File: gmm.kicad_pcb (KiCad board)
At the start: 6 copper layers, 55 x 50 mm, 212 parts, among them P1 10144518-061802LF, P2 10144518-061802LF, P3 10144518-061802LF, P4 10144518-101802LF, U1 CCGM1A1, U10 PCA9539AHF, U11 TPS3840DL28DBV, U2 5P49V6965, U3 LM26480SQ, U4 STG3692, U5 STG3692, U6 74LVC1G08, U7 74LVC1G07, U8 STG3692, U9 IS25LQ032B-JNLE, Y1 NX3225SA

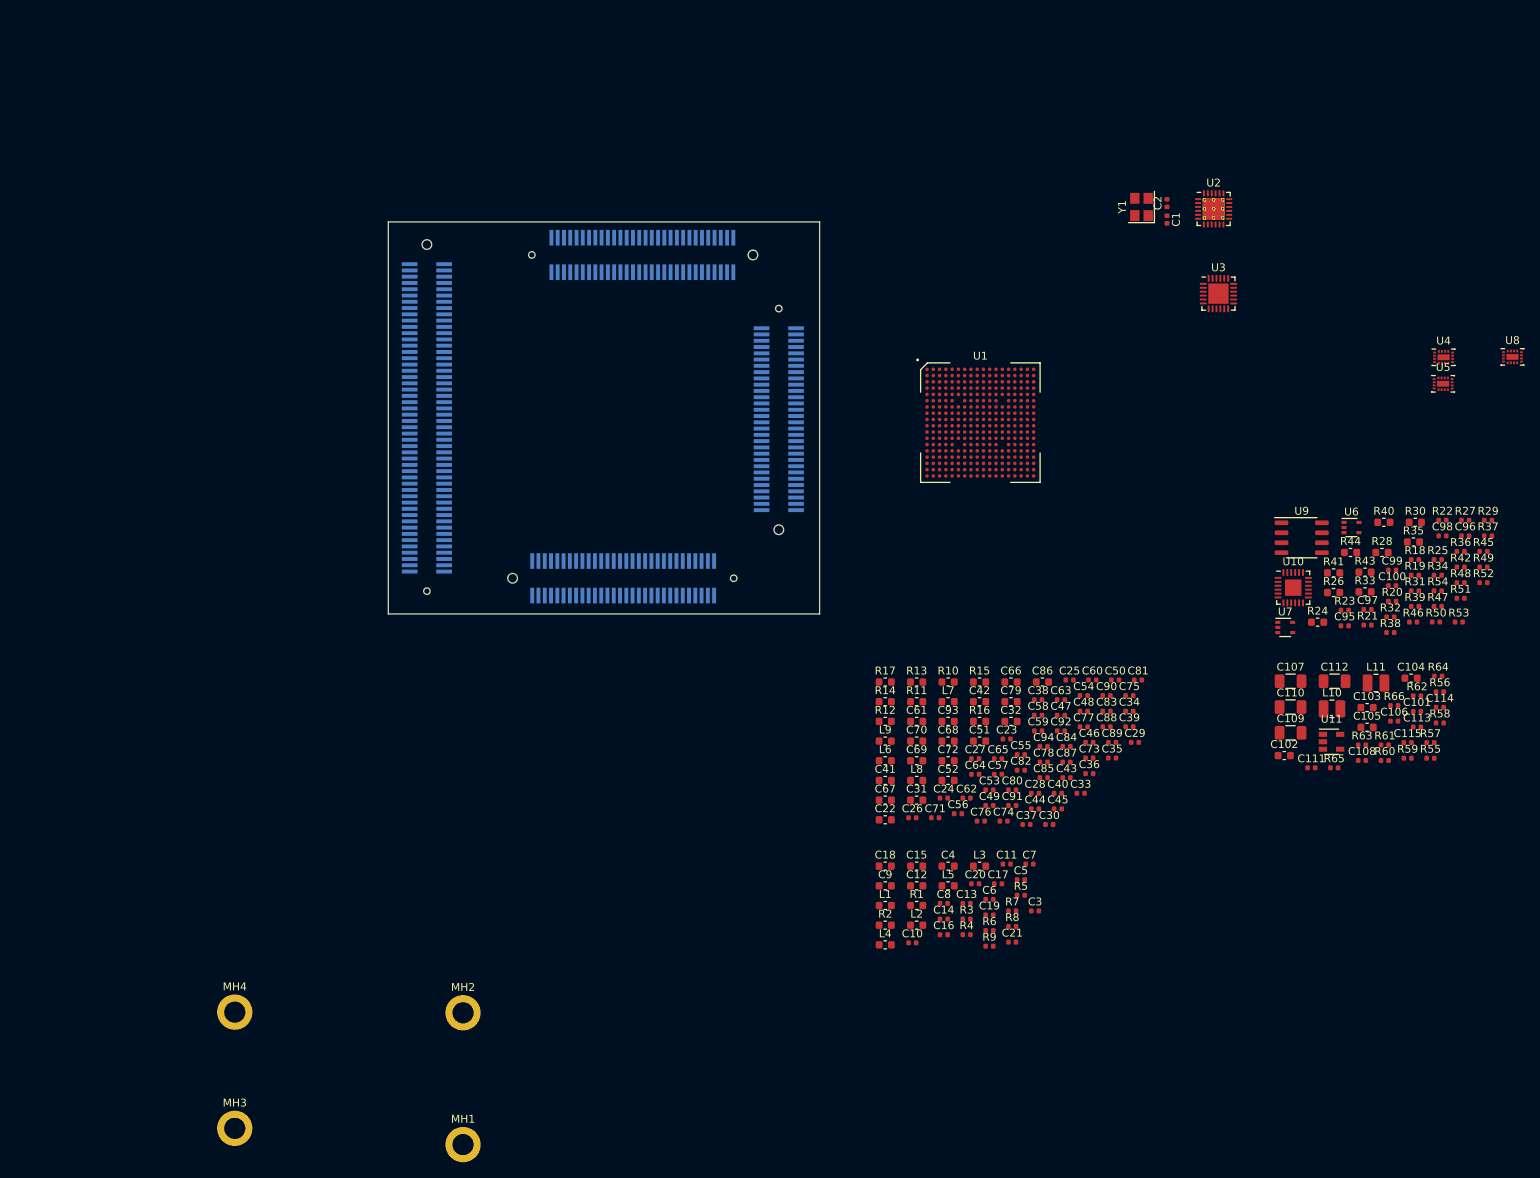
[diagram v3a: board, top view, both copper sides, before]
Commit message: Switch to five identical connectors, draft IO connection, current working PCB size is 50 x 75 mm
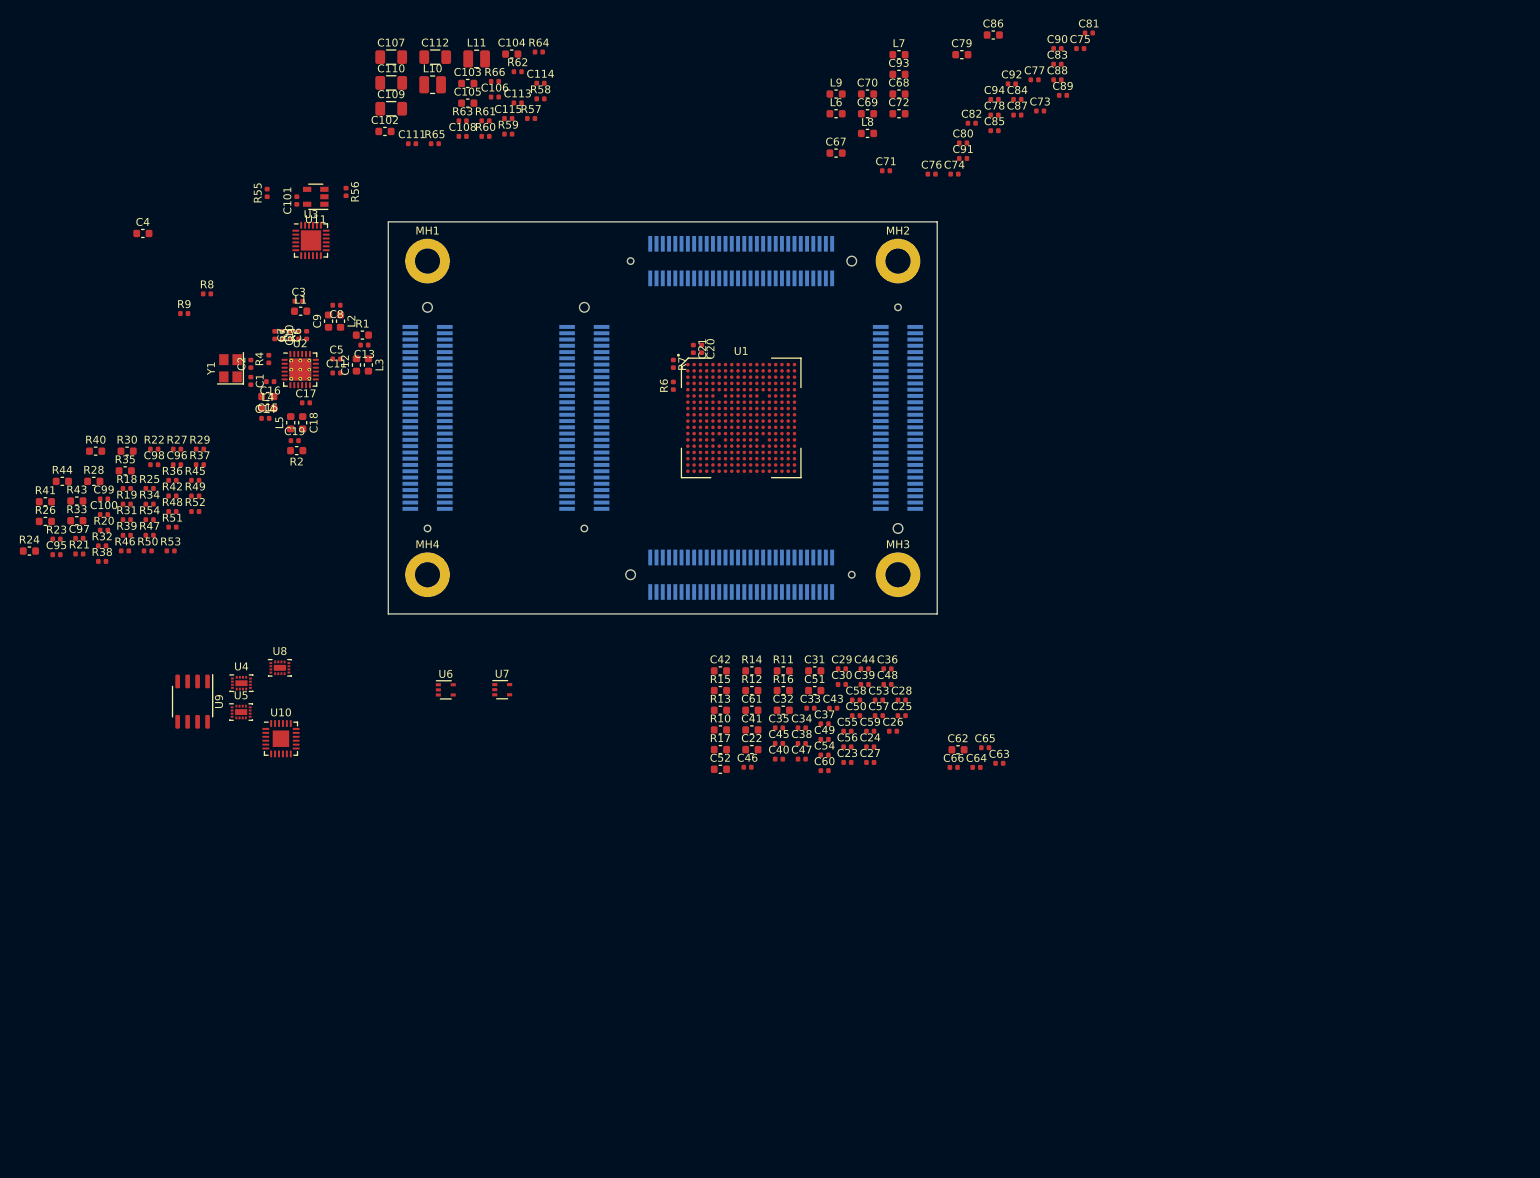
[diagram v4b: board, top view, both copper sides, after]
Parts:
- added P5: 10144518-061802LF, Amphenol:10144518-061802LF, B.Cu at (95.0, 105.0)
- C62: value 0.01uF -> 1.0uF; footprint Capacitor_SMD:C_0402_1005Metric -> Capacitor_SMD:C_0603_1608Metric
- C66: value 1.0uF -> 0.01uF; footprint Capacitor_SMD:C_0603_1608Metric -> Capacitor_SMD:C_0402_1005Metric
- MH1, MH2, MH3, MH4: footprint MountingHole:MountingHole_2.7mm_M2.5_ISO14580_Pad -> MountingHole:MountingHole_3.2mm_M3_ISO7380_Pad
- P4: value 10144518-101802LF -> 10144518-061802LF; footprint Amphenol:10144518-101802LF -> Amphenol:10144518-061802LF
- moved R55 164.9 mm to (74.5, 76.3), turned to 90 degrees
- moved R50 164.5 mm to (59.3, 122.0)
- moved C100 164.5 mm to (53.7, 117.3)
- moved C95 164.5 mm to (47.7, 122.4)
- moved C96 164.5 mm to (63.1, 111.0)
- moved C97 164.5 mm to (50.6, 120.4)
- moved C98 164.5 mm to (60.1, 111.0)
- moved C99 164.5 mm to (53.7, 115.3)
- moved R18 164.5 mm to (56.6, 114.0)
- moved R19 164.5 mm to (56.6, 116.0)
- moved R20 164.5 mm to (53.7, 119.3)
- moved R21 164.5 mm to (50.6, 122.3)
- moved R22 164.5 mm to (60.1, 109.0)
- moved R23 164.5 mm to (47.7, 120.5)
- moved R24 164.5 mm to (44.2, 122.0)
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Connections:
- C22 pad 1: VIO_N1 -> VIO_W1
- C23 pad 1: VIO_N1 -> VIO_W1
- C24 pad 1: VIO_N1 -> VIO_W1
- C25 pad 1: VIO_N1 -> VIO_W1
- C26 pad 1: VIO_N1 -> VIO_W1
- C27 pad 1: VIO_E1 -> VIO_W2
- C28 pad 1: VIO_E1 -> VIO_W2
- C29 pad 1: VIO_E1 -> VIO_W2
- C30 pad 1: VIO_E1 -> VIO_W2
- C31 pad 1: VIO_E1 -> VIO_W2
- C32 pad 1: VIO_N2 -> VIO_N1
- C33 pad 1: VIO_N2 -> VIO_N1
- C34 pad 1: VIO_N2 -> VIO_N1
- C35 pad 1: VIO_N2 -> VIO_N1
- C36 pad 1: VIO_N2 -> VIO_N1
- C37 pad 1: VIO_E2 -> VIO_N2
- C38 pad 1: VIO_E2 -> VIO_N2
- C39 pad 1: VIO_E2 -> VIO_N2
- C40 pad 1: VIO_E2 -> VIO_N2
- C41 pad 1: VIO_E2 -> VIO_N2
- C42 pad 1: VIO_W1 -> VIO_E1
- C43 pad 1: VIO_W1 -> VIO_E1
- C44 pad 1: VIO_W1 -> VIO_E1
- C45 pad 1: VIO_W1 -> VIO_E1
- C46 pad 1: VIO_W1 -> VIO_E1
- C47 pad 1: VIO_S1 -> VIO_E2
- C48 pad 1: VIO_S1 -> VIO_E2
- C49 pad 1: VIO_S1 -> VIO_E2
- C50 pad 1: VIO_S1 -> VIO_E2
- C51 pad 1: VIO_S1 -> VIO_E2
- C52 pad 1: VIO_W2 -> VIO_S1
- C53 pad 1: VIO_W2 -> VIO_S1
- C54 pad 1: VIO_W2 -> VIO_S1
- C55 pad 1: VIO_W2 -> VIO_S1
- C56 pad 1: VIO_W2 -> VIO_S1
- P1 pad 1: (no net) -> GND
- P1 pad 10: (no net) -> IO_N1_A2
- P1 pad 11: (no net) -> IO_N1_B3
- P1 pad 12: (no net) -> IO_N1_B2
- P1 pad 13: (no net) -> GND
- P1 pad 14: (no net) -> GND
- P1 pad 15: (no net) -> IO_N1_A5
- P1 pad 16: (no net) -> IO_N1_A4
- P1 pad 17: (no net) -> IO_N1_B5
- P1 pad 18: (no net) -> IO_N1_B4
- P1 pad 19: (no net) -> GND
- P1 pad 2: (no net) -> GND
- P1 pad 20: (no net) -> GND
- P1 pad 21: (no net) -> IO_N1_A7
- P1 pad 22: (no net) -> IO_N1_A6
- P1 pad 23: (no net) -> IO_N1_B7
- P1 pad 24: (no net) -> IO_N1_B6
- P1 pad 25: (no net) -> GND
- P1 pad 26: (no net) -> GND
- P1 pad 27: (no net) -> IO_N2_B0
- P1 pad 28: (no net) -> IO_N1_A8
- P1 pad 29: (no net) -> IO_N2_A0
- P1 pad 3: (no net) -> IO_N1_A1
- P1 pad 30: (no net) -> IO_N1_B8
- P1 pad 31: (no net) -> VIO_N1
- P1 pad 32: (no net) -> VIO_N1
- P1 pad 33: (no net) -> +2V5
- P1 pad 34: (no net) -> +2V5
- P1 pad 35: (no net) -> VIO_N2
- P1 pad 36: (no net) -> VIO_N2
- P1 pad 37: (no net) -> IO_N2_B2
- P1 pad 38: (no net) -> IO_N2_B1
- P1 pad 39: (no net) -> IO_N2_A2
- P1 pad 4: (no net) -> IO_N1_A0
- P1 pad 40: (no net) -> IO_N2_A1
- P1 pad 41: (no net) -> GND
- P1 pad 42: (no net) -> GND
- P1 pad 43: (no net) -> IO_N2_B4
- P1 pad 44: (no net) -> IO_N2_B3
- P1 pad 45: (no net) -> IO_N2_A4
- P1 pad 46: (no net) -> IO_N2_A3
- P1 pad 47: (no net) -> GND
- P1 pad 48: (no net) -> GND
- P1 pad 49: (no net) -> IO_N2_B6
- P1 pad 5: (no net) -> IO_N1_B1
- P1 pad 50: (no net) -> IO_N2_B5
- P1 pad 51: (no net) -> IO_N2_A6
- P1 pad 52: (no net) -> IO_N2_A5
- P1 pad 53: (no net) -> GND
- P1 pad 54: (no net) -> GND
- P1 pad 55: (no net) -> IO_N2_B8
- P1 pad 56: (no net) -> IO_N2_B7
- P1 pad 57: (no net) -> IO_N2_A8
- P1 pad 58: (no net) -> IO_N2_A7
- P1 pad 59: (no net) -> GND
- P1 pad 6: (no net) -> IO_N1_B0
- P1 pad 60: (no net) -> GND
- P1 pad 7: (no net) -> GND
- P1 pad 8: (no net) -> GND
- P1 pad 9: (no net) -> IO_N1_A3
- P2 pad 1: (no net) -> GND
- P2 pad 10: (no net) -> IO_E2_B5
- P2 pad 11: (no net) -> IO_E2_A6
- P2 pad 12: (no net) -> IO_E2_A5
- P2 pad 13: (no net) -> GND
- P2 pad 14: (no net) -> GND
- P2 pad 15: (no net) -> IO_E2_B4
- P2 pad 16: (no net) -> IO_E2_B3
- P2 pad 17: (no net) -> IO_E2_A4
- P2 pad 18: (no net) -> IO_E2_A3
- P2 pad 19: (no net) -> GND
- P2 pad 2: (no net) -> GND
- P2 pad 20: (no net) -> GND
- P2 pad 21: (no net) -> IO_E2_B2
- P2 pad 22: (no net) -> IO_E2_A1
- P2 pad 23: (no net) -> IO_E2_A2
- P2 pad 24: (no net) -> IO_E2_B1
- P2 pad 25: (no net) -> GND
- P2 pad 26: (no net) -> GND
- P2 pad 27: (no net) -> IO_E2_B0
- P2 pad 28: (no net) -> IO_E1_B8
- P2 pad 29: (no net) -> IO_E2_A0
- P2 pad 3: (no net) -> IO_E2_B8
- P2 pad 30: (no net) -> IO_E1_A8
- P2 pad 31: (no net) -> VIO_E2
- P2 pad 32: (no net) -> VIO_E2
- P2 pad 33: (no net) -> +2V5
- P2 pad 34: (no net) -> +2V5
- P2 pad 35: (no net) -> VIO_E1
- P2 pad 36: (no net) -> VIO_E1
- P2 pad 37: (no net) -> IO_E1_B7
- P2 pad 38: (no net) -> IO_E1_B6
- P2 pad 39: (no net) -> IO_E1_A7
- P2 pad 4: (no net) -> IO_E2_B7
- P2 pad 40: (no net) -> IO_E1_A6
- P2 pad 41: (no net) -> GND
- P2 pad 42: (no net) -> GND
- P2 pad 43: (no net) -> IO_E1_B5
- P2 pad 44: (no net) -> IO_E1_B4
- P2 pad 45: (no net) -> IO_E1_A5
- P2 pad 46: (no net) -> IO_E1_A4
- P2 pad 47: (no net) -> GND
- P2 pad 48: (no net) -> GND
- P2 pad 49: (no net) -> IO_E1_B3
- P2 pad 5: (no net) -> IO_E2_A8
- P2 pad 50: (no net) -> IO_E1_B2
- P2 pad 51: (no net) -> IO_E1_A3
- P2 pad 52: (no net) -> IO_E1_A2
- P2 pad 53: (no net) -> GND
- P2 pad 54: (no net) -> GND
- P2 pad 55: (no net) -> IO_E1_B1
- P2 pad 56: (no net) -> IO_E1_B0
- P2 pad 57: (no net) -> IO_E1_A1
- P2 pad 58: (no net) -> IO_E1_A0
- P2 pad 59: (no net) -> GND
- P2 pad 6: (no net) -> IO_E2_A7
- P2 pad 60: (no net) -> GND
- P2 pad 7: (no net) -> GND
- P2 pad 8: (no net) -> GND
- P2 pad 9: (no net) -> IO_E2_B6
- P3 pad 1: (no net) -> GND
- P3 pad 10: (no net) -> IO_S2_A7
- P3 pad 11: (no net) -> IO_S2_A4
- P3 pad 12: (no net) -> IO_S2_B7
- P3 pad 13: (no net) -> GND
- P3 pad 14: (no net) -> GND
- P3 pad 15: (no net) -> IO_S2_B2
- P3 pad 16: (no net) -> IO_S2_A5
- P3 pad 17: (no net) -> IO_S2_A2
- P3 pad 18: (no net) -> IO_S2_B5
- P3 pad 19: (no net) -> GND
- P3 pad 2: (no net) -> GND
- P3 pad 20: (no net) -> GND
- P3 pad 21: (no net) -> IO_S2_B0
- P3 pad 22: (no net) -> IO_S2_A3
- P3 pad 23: (no net) -> IO_S2_A0
- P3 pad 24: (no net) -> IO_S2_B3
- P3 pad 25: (no net) -> GND
- P3 pad 26: (no net) -> GND
- P3 pad 28: (no net) -> IO_S1_B8
- P3 pad 3: (no net) -> IO_S2_B6
- P3 pad 30: (no net) -> IO_S1_A8
- P3 pad 31: (no net) -> VIO_S2
- P3 pad 32: (no net) -> VIO_S2
- P3 pad 33: (no net) -> +2V5
- P3 pad 34: (no net) -> +2V5
- P3 pad 35: (no net) -> VIO_S1
- P3 pad 36: (no net) -> VIO_S1
- P3 pad 37: (no net) -> IO_S1_A6
- P3 pad 38: (no net) -> IO_S1_B7
- P3 pad 39: (no net) -> IO_S1_B6
- P3 pad 4: (no net) -> IO_S2_A8
- P3 pad 40: (no net) -> IO_S1_A7
- P3 pad 41: (no net) -> GND
- P3 pad 42: (no net) -> GND
- P3 pad 43: (no net) -> IO_S1_B4
- P3 pad 44: (no net) -> IO_S1_B5
- P3 pad 45: (no net) -> IO_S1_A4
- P3 pad 46: (no net) -> IO_S1_A5
- P3 pad 47: (no net) -> GND
- P3 pad 48: (no net) -> GND
- P3 pad 49: (no net) -> IO_S1_B2
- P3 pad 5: (no net) -> IO_S2_A6
- P3 pad 50: (no net) -> IO_S1_B3
- P3 pad 51: (no net) -> IO_S1_A2
- P3 pad 52: (no net) -> IO_S1_A3
- P3 pad 53: (no net) -> GND
- P3 pad 54: (no net) -> GND
- P3 pad 55: (no net) -> IO_S1_B0
- P3 pad 56: (no net) -> IO_S1_B1
- P3 pad 57: (no net) -> IO_S1_A0
- P3 pad 58: (no net) -> IO_S1_A1
- P3 pad 59: (no net) -> GND
- P3 pad 6: (no net) -> IO_S2_B8
- P3 pad 60: (no net) -> GND
- P3 pad 7: (no net) -> GND
- P3 pad 8: (no net) -> GND
- P3 pad 9: (no net) -> IO_S2_B4
- P4 pad 1: (no net) -> GND
- P4 pad 10: (no net) -> IO_W1_A2
- P4 pad 11: (no net) -> IO_W1_A3
- P4 pad 12: (no net) -> IO_W1_B2
- P4 pad 13: (no net) -> GND
- P4 pad 14: (no net) -> GND
- P4 pad 15: (no net) -> IO_W1_B4
- P4 pad 16: (no net) -> IO_W1_A5
- P4 pad 17: (no net) -> IO_W1_A4
- P4 pad 18: (no net) -> IO_W1_B5
- P4 pad 19: (no net) -> GND
- P4 pad 2: (no net) -> GND
- P4 pad 20: (no net) -> GND
- P4 pad 21: (no net) -> IO_W1_B6
- P4 pad 22: (no net) -> IO_W1_A7
- P4 pad 23: (no net) -> IO_W1_A6
- P4 pad 24: (no net) -> IO_W1_B7
- P4 pad 25: (no net) -> GND
- P4 pad 26: (no net) -> GND
- P4 pad 27: (no net) -> IO_W1_B8
- P4 pad 28: (no net) -> IO_W2_A0
- P4 pad 29: (no net) -> IO_W1_A8
- P4 pad 3: (no net) -> IO_W1_B1
- P4 pad 30: (no net) -> IO_W2_B0
- P4 pad 31: (no net) -> VIO_W1
- P4 pad 32: (no net) -> VIO_W1
- P4 pad 33: (no net) -> +2V5
- P4 pad 34: (no net) -> +2V5
- P4 pad 35: (no net) -> VIO_W2
- P4 pad 36: (no net) -> VIO_W2
- P4 pad 37: (no net) -> IO_W2_B2
- P4 pad 38: (no net) -> IO_W2_B1
- P4 pad 39: (no net) -> IO_W2_A2
- P4 pad 4: (no net) -> IO_W1_A0
- P4 pad 40: (no net) -> IO_W2_A1
- P4 pad 41: (no net) -> GND
- P4 pad 42: (no net) -> GND
- P4 pad 43: (no net) -> IO_W2_B4
- P4 pad 44: (no net) -> IO_W2_B3
- P4 pad 45: (no net) -> IO_W2_A4
- P4 pad 46: (no net) -> IO_W2_A3
- P4 pad 47: (no net) -> GND
- P4 pad 48: (no net) -> GND
- P4 pad 49: (no net) -> IO_W2_B6
- P4 pad 5: (no net) -> IO_W1_A1
- P4 pad 50: (no net) -> IO_W2_B5
- P4 pad 51: (no net) -> IO_W2_A6
- P4 pad 52: (no net) -> IO_W2_A5
- P4 pad 53: (no net) -> GND
- P4 pad 54: (no net) -> GND
- P4 pad 55: (no net) -> IO_W2_B8
- P4 pad 56: (no net) -> IO_W2_B7
- P4 pad 57: (no net) -> IO_W2_A8
- P4 pad 58: (no net) -> IO_W2_A7
- P4 pad 59: (no net) -> GND
- P4 pad 6: (no net) -> IO_W1_B0
- P4 pad 60: (no net) -> GND
- P4 pad 7: (no net) -> GND
- P4 pad 8: (no net) -> GND
- P4 pad 9: (no net) -> IO_W1_B3
- R10 pad 2: VIO_N1 -> VIO_W1
- R11 pad 2: VIO_E1 -> VIO_W2
- R12 pad 2: VIO_N2 -> VIO_N1
- R13 pad 2: VIO_E2 -> VIO_N2
- R14 pad 2: VIO_W1 -> VIO_E1
- R15 pad 2: VIO_S1 -> VIO_E2
- R16 pad 2: VIO_W2 -> VIO_S1
- U1 pad A10: (no net) -> IO_N2_A1
- U1 pad A11: (no net) -> IO_N2_A3
- U1 pad A13: (no net) -> IO_N2_A5
- U1 pad A14: (no net) -> IO_N2_A7
- U1 pad A15: (no net) -> IO_E2_B8
- U1 pad A16: (no net) -> IO_E2_B7
- U1 pad A17: (no net) -> IO_E2_A7
- U1 pad A5: (no net) -> IO_N1_A2
- U1 pad A6: (no net) -> IO_N1_A3
- U1 pad A8: (no net) -> IO_N1_A6
- U1 pad A9: (no net) -> IO_N1_A8
- U1 pad B10: (no net) -> IO_N2_B1
- U1 pad B11: (no net) -> IO_N2_B3
- U1 pad B13: (no net) -> IO_N2_B5
- U1 pad B14: (no net) -> IO_N2_B7
- U1 pad B15: (no net) -> IO_E2_A8
- U1 pad B18: (no net) -> IO_E2_B6
- U1 pad B3: Net-(C79-Pad1) -> Net-(C72-Pad1)
- U1 pad B4: (no net) -> IO_N1_B0
- U1 pad B5: (no net) -> IO_N1_B2
- U1 pad B6: (no net) -> IO_N1_B3
- U1 pad B8: (no net) -> IO_N1_B6
- U1 pad B9: (no net) -> IO_N1_B8
- U1 pad C10: (no net) -> IO_N2_B0
- U1 pad C11: (no net) -> IO_N2_B2
- U1 pad C13: (no net) -> IO_N2_B4
- U1 pad C14: (no net) -> IO_N2_B6
- U1 pad C15: (no net) -> IO_N2_B8
- U1 pad C16: (no net) -> IO_E2_A5
- U1 pad C17: (no net) -> IO_E2_B5
- U1 pad C18: (no net) -> IO_E2_A6
- U1 pad C2: Net-(C72-Pad1) -> Net-(C79-Pad1)
- U1 pad C4: (no net) -> IO_N1_A0
- U1 pad C5: (no net) -> IO_N1_B1
- U1 pad C7: (no net) -> IO_N1_B4
- U1 pad C8: (no net) -> IO_N1_B5
- U1 pad C9: (no net) -> IO_N1_B7
- U1 pad D10: (no net) -> IO_N2_A0
- U1 pad D11: (no net) -> IO_N2_A2
- U1 pad D13: (no net) -> IO_N2_A4
- U1 pad D14: (no net) -> IO_N2_A6
- U1 pad D15: (no net) -> IO_N2_A8
- U1 pad D17: (no net) -> IO_E2_B4
- U1 pad D18: (no net) -> IO_E2_A4
- U1 pad D5: (no net) -> IO_N1_A1
- U1 pad D7: (no net) -> IO_N1_A4
- U1 pad D8: (no net) -> IO_N1_A5
- U1 pad D9: (no net) -> IO_N1_A7
- U1 pad F1: (no net) -> IO_W2_B7
- U1 pad F15: (no net) -> IO_E2_A2
- U1 pad F16: (no net) -> IO_E2_B2
- U1 pad F17: (no net) -> IO_E2_B3
- U1 pad F18: (no net) -> IO_E2_A3
- U1 pad F2: (no net) -> IO_W2_A7
- U1 pad F3: (no net) -> IO_W2_A8
- U1 pad F4: (no net) -> IO_W2_B8
- U1 pad G1: (no net) -> IO_W2_B5
- U1 pad G15: (no net) -> IO_E2_A0
- U1 pad G16: (no net) -> IO_E2_B0
- U1 pad G17: (no net) -> IO_E2_B1
- U1 pad G18: (no net) -> IO_E2_A1
- U1 pad G2: (no net) -> IO_W2_A5
- U1 pad G3: (no net) -> IO_W2_A6
- U1 pad G4: (no net) -> IO_W2_B6
- U1 pad H15: (no net) -> IO_E1_A7
- U1 pad H16: (no net) -> IO_E1_B7
- U1 pad H17: (no net) -> IO_E1_B8
- U1 pad H18: (no net) -> IO_E1_A8
- U1 pad J1: (no net) -> IO_W2_B3
- U1 pad J15: (no net) -> IO_E1_A5
- U1 pad J16: (no net) -> IO_E1_B5
- U1 pad J17: (no net) -> IO_E1_B6
- U1 pad J18: (no net) -> IO_E1_A6
- U1 pad J2: (no net) -> IO_W2_A3
- U1 pad J3: (no net) -> IO_W2_A4
- U1 pad J4: (no net) -> IO_W2_B4
- U1 pad K1: (no net) -> IO_W2_B1
- U1 pad K2: (no net) -> IO_W2_A1
- U1 pad K3: (no net) -> IO_W2_A2
- U1 pad K4: (no net) -> IO_W2_B2
- U1 pad L1: (no net) -> IO_W2_B0
- U1 pad L15: (no net) -> IO_E1_A3
- U1 pad L16: (no net) -> IO_E1_B3
- U1 pad L17: (no net) -> IO_E1_B4
- U1 pad L18: (no net) -> IO_E1_A4
- U1 pad L2: (no net) -> IO_W2_A0
- U1 pad L3: (no net) -> IO_W1_A8
- U1 pad L4: (no net) -> IO_W1_B8
- U1 pad M1: (no net) -> IO_W1_B7
- U1 pad M15: (no net) -> IO_E1_A1
- U1 pad M16: (no net) -> IO_E1_B1
- U1 pad M17: (no net) -> IO_E1_B2
- U1 pad M18: (no net) -> IO_E1_A2
- U1 pad M2: (no net) -> IO_W1_A7
- U1 pad M3: (no net) -> IO_W1_A6
- U1 pad M4: (no net) -> IO_W1_B6
- U1 pad N1: (no net) -> IO_W1_B5
- U1 pad N15: (no net) -> IO_E1_A0
- U1 pad N16: (no net) -> IO_E1_B0
- U1 pad N17: (no net) -> IO_S2_B8
- U1 pad N18: (no net) -> IO_S2_A8
- U1 pad N2: (no net) -> IO_W1_A5
- U1 pad N3: (no net) -> IO_W1_A4
- U1 pad N4: (no net) -> IO_W1_B4
- U1 pad P15: (no net) -> IO_S2_A6
- U1 pad P16: (no net) -> IO_S2_B6
- U1 pad P17: (no net) -> IO_S2_B7
- U1 pad P18: (no net) -> IO_S2_A7
- U1 pad P5: (no net) -> IO_W1_B3
- U1 pad R1: (no net) -> IO_W1_B2
- U1 pad R10: (no net) -> IO_S1_A2
- U1 pad R12: (no net) -> IO_S1_A4
- U1 pad R13: (no net) -> IO_S1_A6
- U1 pad R14: (no net) -> IO_S2_A0
- U1 pad R15: (no net) -> IO_S2_A2
- U1 pad R2: (no net) -> IO_W1_A2
- U1 pad R3: (no net) -> IO_W1_B1
- U1 pad R4: (no net) -> IO_W1_A1
- U1 pad R5: (no net) -> IO_W1_A3
- U1 pad R9: (no net) -> IO_S1_A0
- U1 pad T1: (no net) -> IO_W1_B0
- U1 pad T10: (no net) -> IO_S1_B2
- U1 pad T12: (no net) -> IO_S1_B4
- U1 pad T13: (no net) -> IO_S1_B6
- U1 pad T14: (no net) -> IO_S2_B0
- U1 pad T15: (no net) -> IO_S2_B2
- U1 pad T16: (no net) -> IO_S2_A4
- U1 pad T17: (no net) -> IO_S2_B4
- U1 pad T18: (no net) -> IO_S2_B5
- U1 pad T2: (no net) -> IO_W1_A0
- U1 pad T9: (no net) -> IO_S1_B0
- U1 pad U10: (no net) -> IO_S1_B3
- U1 pad U12: (no net) -> IO_S1_B5
- U1 pad U13: (no net) -> IO_S1_B7
- U1 pad U14: (no net) -> IO_S1_B8
- U1 pad U18: (no net) -> IO_S2_A5
- U1 pad U9: (no net) -> IO_S1_B1
- U1 pad V10: (no net) -> IO_S1_A3
- U1 pad V12: (no net) -> IO_S1_A5
- U1 pad V13: (no net) -> IO_S1_A7
- U1 pad V14: (no net) -> IO_S1_A8
- U1 pad V16: (no net) -> IO_S2_A3
- U1 pad V17: (no net) -> IO_S2_B3
- U1 pad V9: (no net) -> IO_S1_A1
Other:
- board size 55 x 50 mm -> 70 x 50 mm

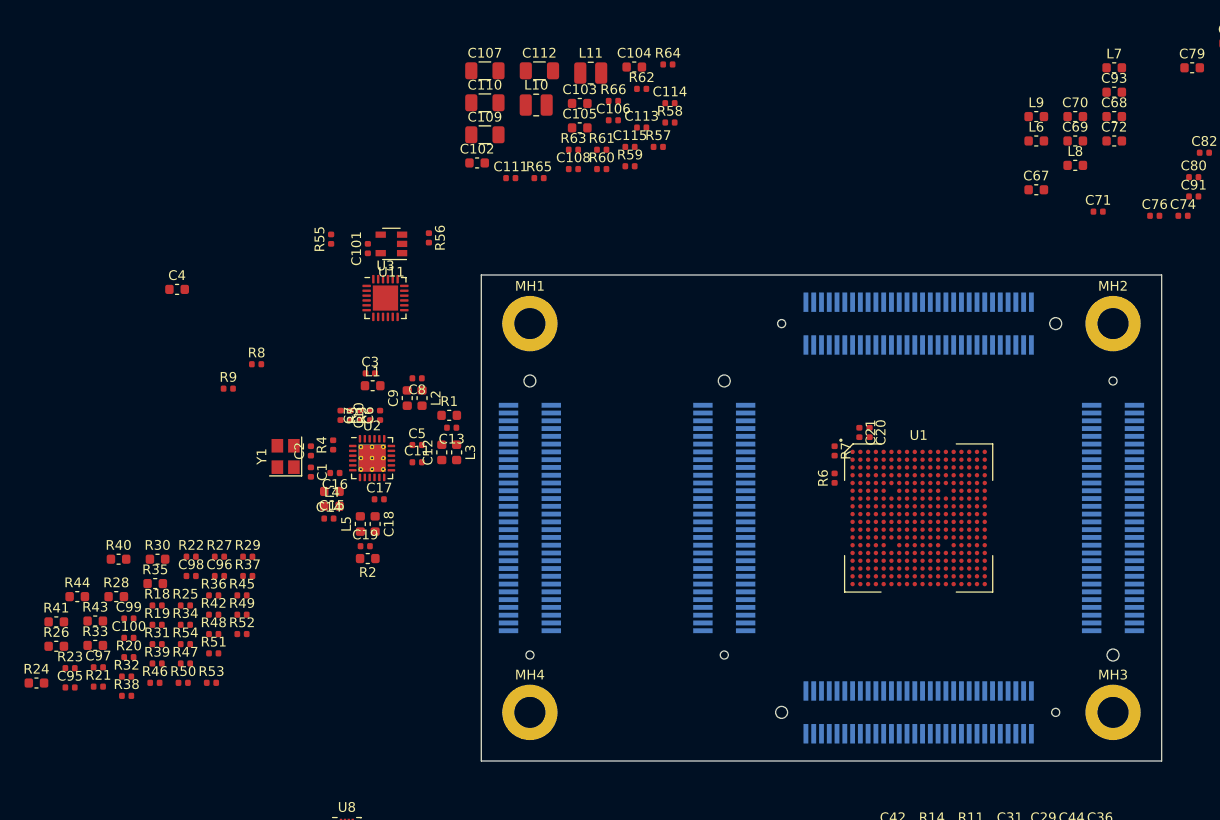
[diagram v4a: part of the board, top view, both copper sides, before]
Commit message: BOM clean-up: unified R/C values and footprints
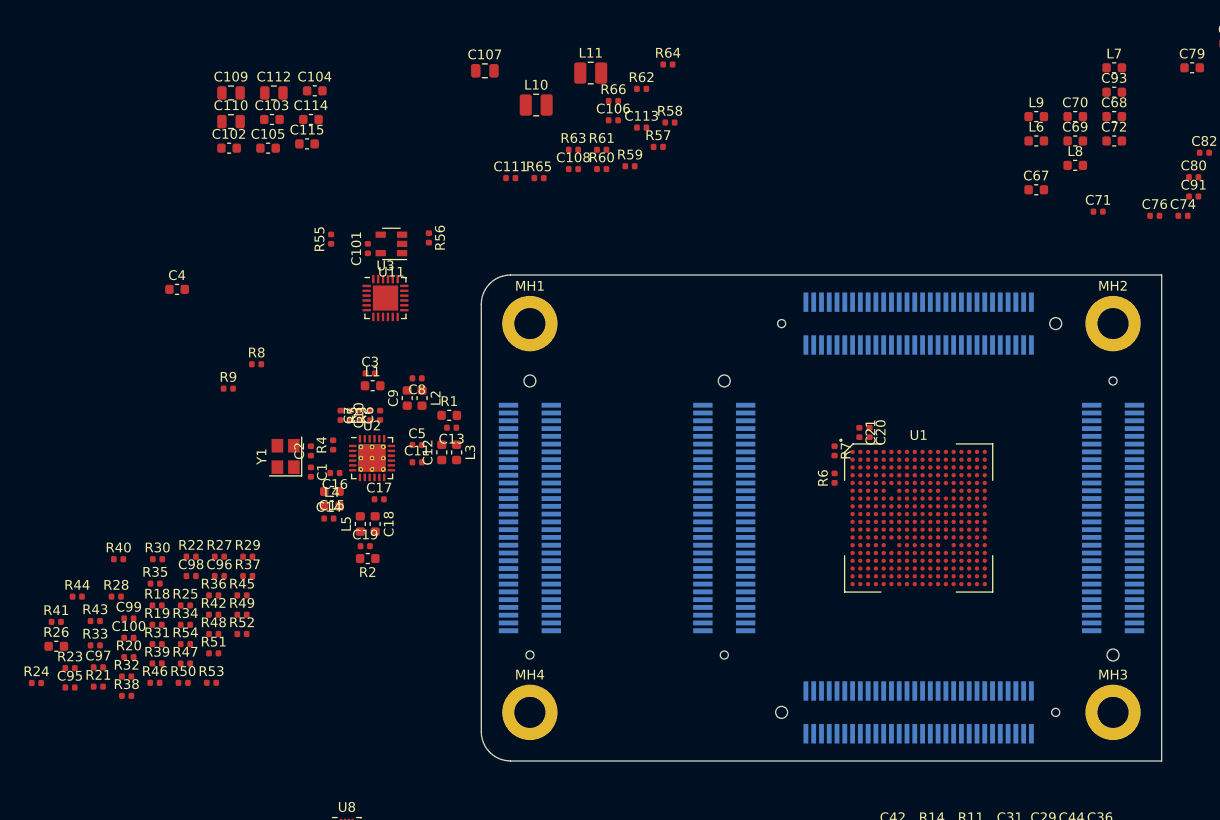
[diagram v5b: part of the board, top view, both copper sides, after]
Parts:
- C102, C103, C104, C105: value 1uF -> 1.0uF
- C107, C109, C110, C112: footprint Capacitor_SMD:C_1206_3216Metric -> Capacitor_SMD:C_0805_2012Metric
- C114, C115: value 0.47uF -> 1.0uF; footprint Capacitor_SMD:C_0402_1005Metric -> Capacitor_SMD:C_0603_1608Metric
- R24, R28, R30, R33, R35, R40, R41, R43, R44: footprint Resistor_SMD:R_0603_1608Metric -> Resistor_SMD:R_0402_1005Metric
- moved C114 37.0 mm to (72.5, 64.0)
- moved C115 33.2 mm to (72.1, 66.5)
- moved C104 33.0 mm to (72.9, 61.0)
- moved C105 32.1 mm to (68.1, 67.0)
- moved C103 31.7 mm to (68.5, 64.0)
- moved C112 27.4 mm to (68.7, 61.3)
- moved C109 26.5 mm to (64.2, 61.3)
- moved C110 26.2 mm to (64.2, 64.2)
- moved C102 25.6 mm to (64.0, 67.0)
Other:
- outline, holes or cut-outs redrawn
